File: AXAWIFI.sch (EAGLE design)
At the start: 25 parts, among them IC1 MCP2003, SW1 RESET, SW2 REFLASH

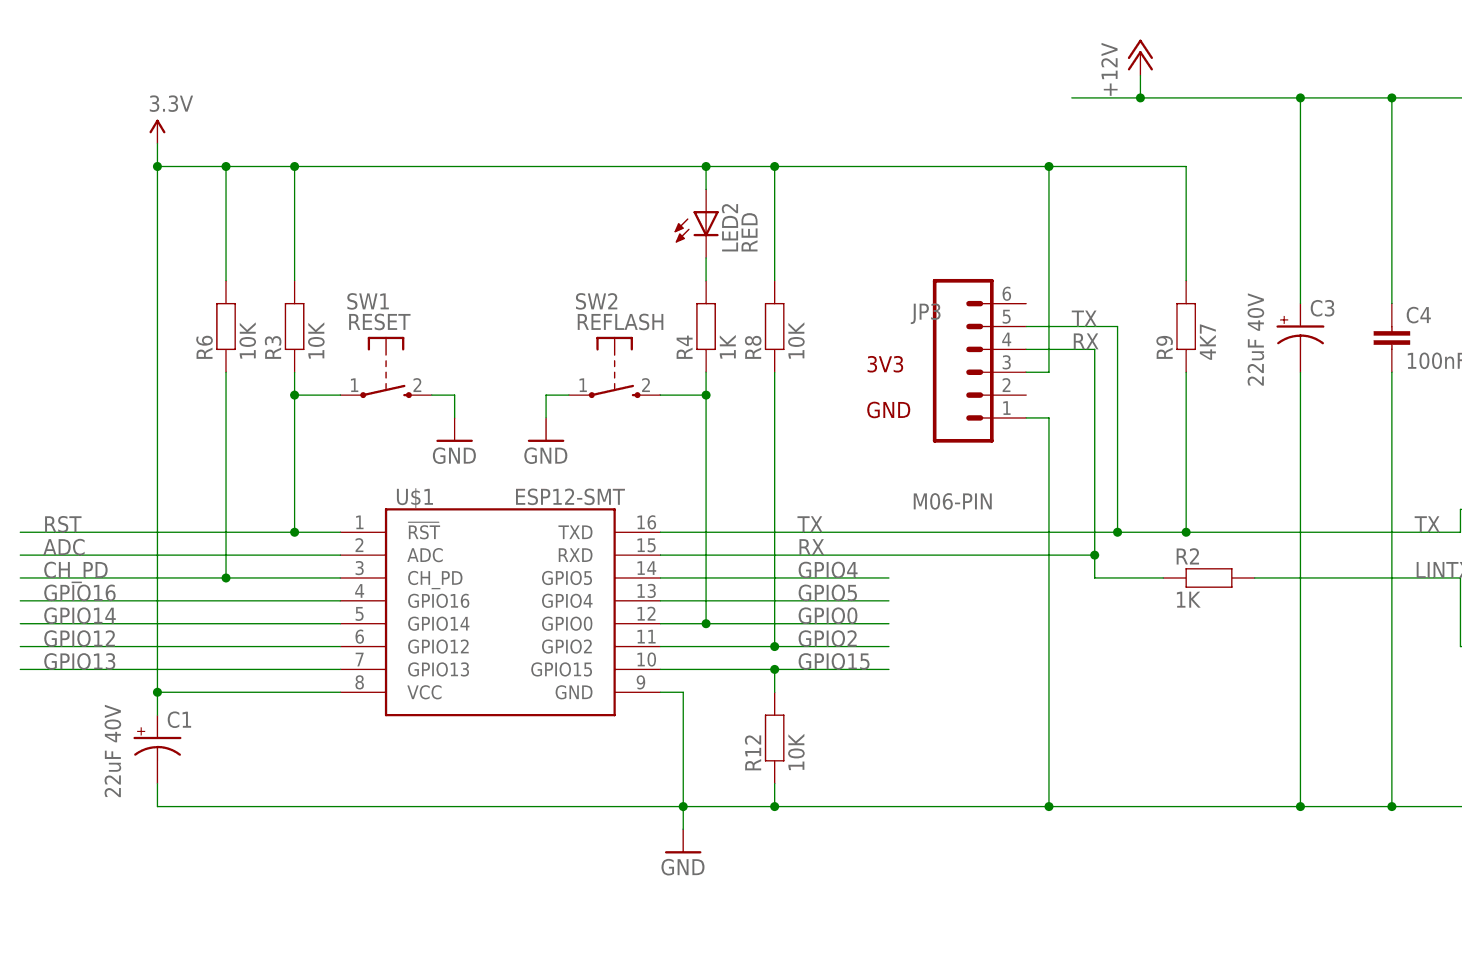
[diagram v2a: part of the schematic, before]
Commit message: Replaced programming header with ESProg header
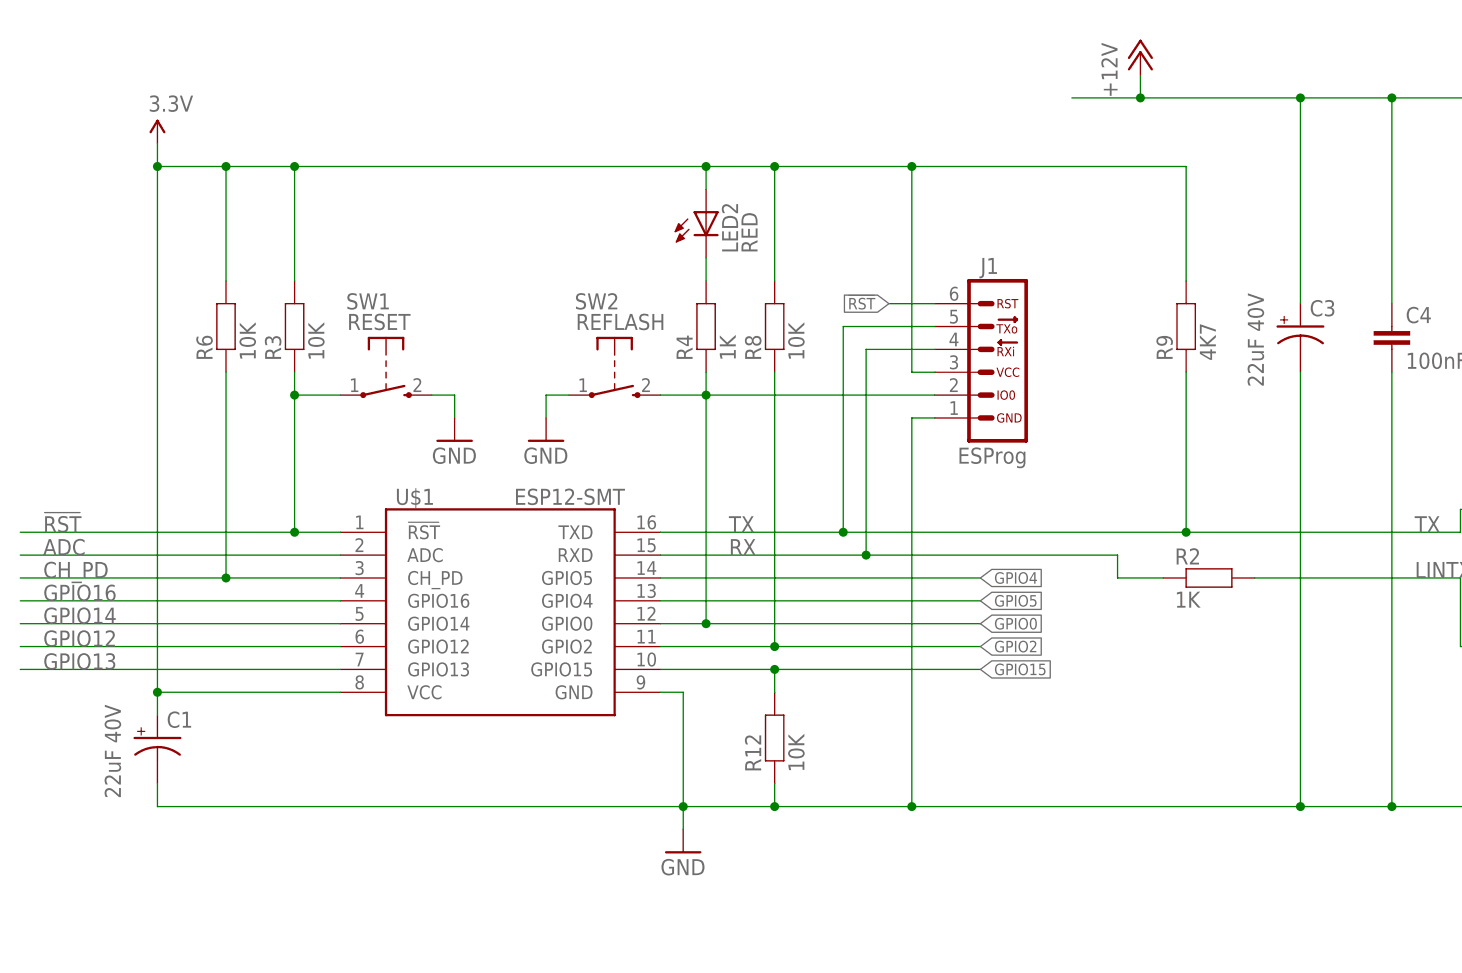
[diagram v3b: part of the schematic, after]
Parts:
- removed JP3: M06-PIN, SuperHouse-Connectors:M06-PIN
- added J1: ESPROG-SOCKET, SuperHouse-Connectors:ESPROG-SOCKET
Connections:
- removed net RST: R3.1, SW1.P, U$1.!RST
- new net !RST: J1.6, R3.1, SW1.P, U$1.!RST
- net 3.3V: now also J1.3; no longer JP3.3
- net GND: now also J1.1; no longer JP3.1
- net GPIO0: now also J1.2
- net RX: now also J1.4; no longer JP3.4
- net TX: now also J1.5; no longer JP3.5
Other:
- note removed: "3V3"
- note removed: "GND"

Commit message: Replace parts using SuperHouse library for 3D models
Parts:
- C1, C3: device analyzer:CPOL-USUD-6,3X5,8 -> SuperHouse-DiscreteSemi:CAP_POLC
- IC1: device freetronics-jon:MCP2003 -> SuperHouse-ICs:MCP2003
- JP2: device freetronics-jon:M03PTH -> SuperHouse-Connectors:M03-PLAIN
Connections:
- net +12V renamed 12V
